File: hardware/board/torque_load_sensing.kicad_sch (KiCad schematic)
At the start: 23 parts, among them J3 Conn_01x05_Female, U10 AD8615, U7 AD8226, U8 ADS7049

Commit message: update schematic annotation
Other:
- note added: "Wheatstone Bridge Inputs Bridge made from 350[Ohm] resistors."
- note removed: "Wheatstone Bridge Inputs"
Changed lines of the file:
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@@
     (effects (font (size 1.27 1.27)) (justify left bottom))
   )
-  (text "Wheatstone\nBridge Inputs" (at 30.48 78.74 0)
+  (text "Wheatstone\nBridge Inputs\n\nBridge made from\n350[Ohm] resistors."
+    (at 30.48 85.725 0)
     (effects (font (size 1.27 1.27)) (justify left bottom))
   )

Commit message: draft v0.1 pcb
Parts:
- added C27 (x2): 100nF, Capacitor_SMD:C_0402_1005Metric, symbol Device:C
- R15: Link https://www.mouser.com/ProductDetail/Vishay-Thin-Film/PTN06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 -> https://www.digikey.com/en/products/detail/panasonic-electr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; Manufacturer (none) -> Panasonic Electronic Components; Manufacturer Number PTN0603E74R1BST1 -> ERA-3AEB4990V; Tolerance (none) -> 0.1%
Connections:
- net GND: now also C27.1, C27.1
- net VREF_1V65: now also C27.2
- net VREF_3V3: now also C27.2
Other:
- note added: "AD8226 Bypass Caps"
- note added: "ADS7049 Bypass Caps"
- note removed: "ADS7049 Bypass Cap"
- moved on the sheet: C24, C26, C27, C58

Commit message: update pcb to v0.2.0
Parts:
- TP1: footprint kicad_component_library:TestPoint_Keystone_5027_Miniature -> TestPoint:TestPoint_THTPad_D3.0mm_Drill1.5mm; Link https://www.digikey.com/en/products/detail/keystone-electro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 -> n/a; Manufacturer Keystone Electronics -> n/a; Manufacturer Number 5027 -> n/a; Notes SMT testpoint with hole for added sturdiness. -> (none)
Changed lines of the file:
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@@
       (effects (font (size 1.27 1.27)) (justify left) hide)
     )
-    (property "Footprint" "kicad_component_library:TestPoint_Keystone_5027_Miniature" (at 197.485 71.12 0)
+    (property "Footprint" "TestPoint:TestPoint_THTPad_D3.0mm_Drill1.5mm" (at 197.485 71.12 0)
       (effects (font (size 1.27 1.27)) hide)
     )
-    (property "Datasheet" "https://www.keyelco.com/userAssets/file/M65p55.pdf" (at 197.485 71.12 0)
+    (property "Datasheet" "n/a" (at 197.485 71.12 0)
       (effects (font (size 1.27 1.27)) hide)
     )
-    (property "Link" "https://www.digikey.com/en/products/detail/keystone-electronics/5027/5118871" (at 192.405 71.12 0)
+    (property "Link" "n/a" (at 192.405 71.12 0)
       (effects (font (size 1.27 1.27)) hide)
     )
-    (property "Notes" "SMT testpoint with hole for added sturdiness." (at 192.405 71.12 0)
+    (property "Notes" "" (at 192.405 71.12 0)
       (effects (font (size 1.27 1.27)) hide)
     )
-    (property "Manufacturer" "Keystone Electronics" (at 192.405 71.12 0)
+    (property "Manufacturer" "n/a" (at 192.405 71.12 0)
       (effects (font (size 1.27 1.27)) hide)
     )
-    (property "Manufacturer Number" "5027" (at 192.405 71.12 0)
+    (property "Manufacturer Number" "n/a" (at 192.405 71.12 0)
       (effects (font (size 1.27 1.27)) hide)
     )

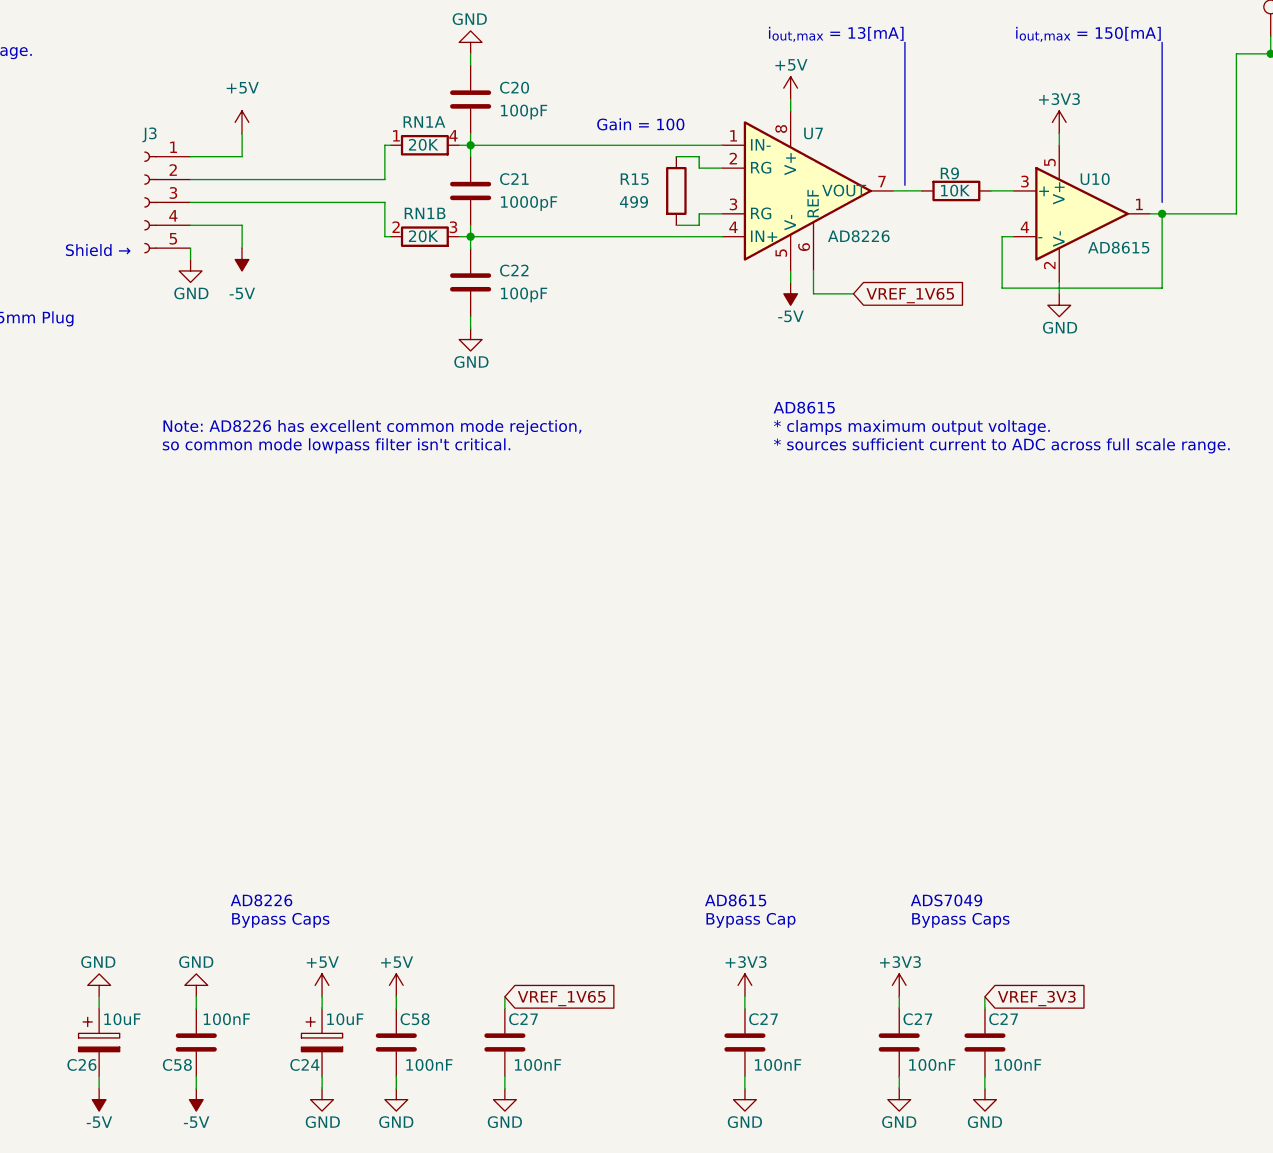
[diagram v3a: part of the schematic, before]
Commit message: update silkscreen size; add mating connector note
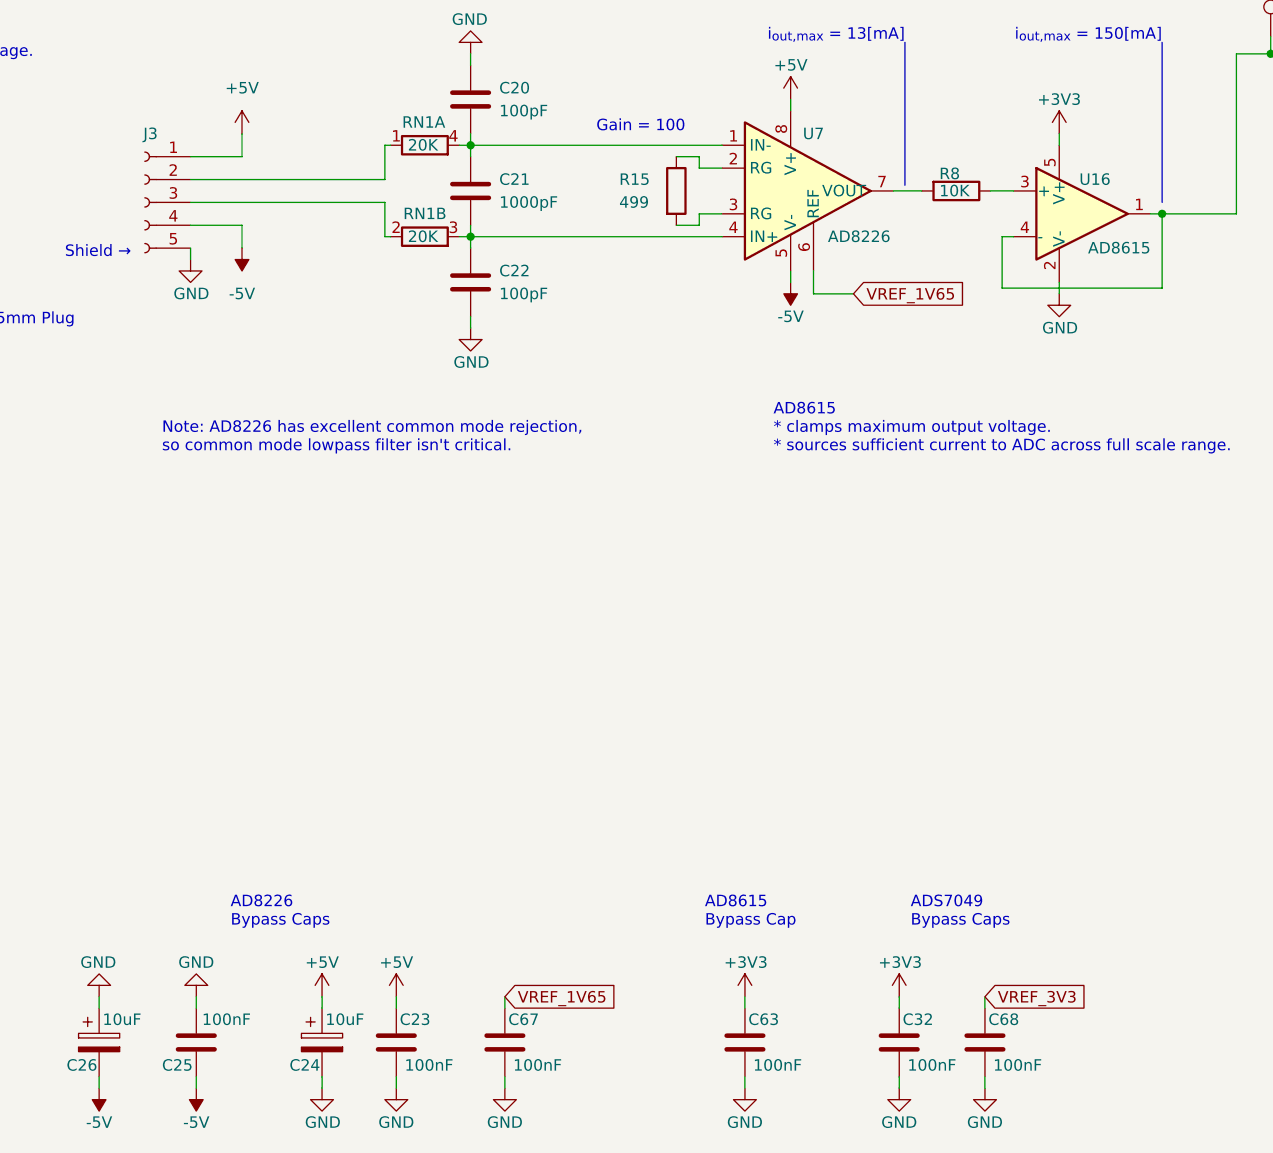
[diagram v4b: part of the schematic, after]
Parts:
- renumbered C58 to C23, C58 to C25, C27 to C32, C27 to C63, C27 to C67, C27 to C68, R9 to R8, U10 to U16

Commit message: update pcb and schematic
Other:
- note added: "Torsional Sensor: RTS-5 or RTS-10 Rated Output: 1.5 [mV/V] https://www.transducertechniques.com/rts-torque-sensor.aspx"
- note added: "±15[mV] full scale range with 10V excitation voltage."
- note removed: "15[mV] full scale range with 10V excitation voltage."
- note removed: "Torsional Sensor: RTS-5 Rated Output: 1.5 [mV/V] https://www.transducertechniques.com/rts-torque-sensor.aspx"
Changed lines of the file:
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@@
 		)
 	)
-	(text "15[mV] full scale range\nwith 10V excitation voltage."
+	(text "±15[mV] full scale range\nwith 10V excitation voltage."
 		(exclude_from_sim no)
-		(at 30.48 73.66 0)
+		(at 30.48 72.39 0)
 		(effects
 			(font
@@
 		)
 	)
-	(text "Torsional Sensor: RTS-5\nRated Output: 1.5 [mV/V]\nhttps://www.transducertechniques.com/rts-torque-sensor.aspx"
+	(text "Torsional Sensor: RTS-5 or RTS-10\nRated Output: 1.5 [mV/V]\nhttps://www.transducertechniques.com/rts-torque-sensor.aspx"
 		(exclude_from_sim no)
 		(at 13.335 20.32 0)
